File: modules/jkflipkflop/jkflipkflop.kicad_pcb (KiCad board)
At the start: 2 copper layers, 52.1 x 53.6 mm, 101 parts, among them J1 Conn_02x18_Counter_Clockwise, Q1 DMP3099L, Q10 2N7002, Q11 DMP3099L, Q12 DMP3099L, Q13 DMP3099L, Q14 2N7002, Q15 2N7002, Q16 2N7002, Q17 DMP3099L, Q18 DMP3099L, Q19 DMP3099L, Q2 2N7002, Q20 2N7002, Q21 2N7002, Q22 2N7002, Q23 DMP3099L, Q24 DMP3099L, Q25 DMP3099L, Q26 2N7002, Q27 2N7002, Q28 2N7002, Q29 DMP3099L, Q3 2N7002, Q30 DMP3099L, Q31 DMP3099L, Q32 2N7002, Q33 2N7002, Q34 2N7002, Q35 DMP3099L, Q36 DMP3099L, Q37 DMP3099L, Q38 2N7002, Q39 2N7002, Q4 2N7002, Q40 2N7002, Q41 DMP3099L, Q42 DMP3099L, Q43 DMP3099L, Q44 2N7002, Q45 2N7002, Q46 2N7002, Q47 DMP3099L, Q48 DMP3099L, Q49 DMP3099L, Q5 DMP3099L, Q50 DMP3099L, Q51 2N7002, Q52 2N7002, Q53 2N7002, Q54 2N7002, Q55 2N7002, Q56 2N7002, Q57 DMP3099L, Q58 DMP3099L, Q59 DMP3099L, Q6 DMP3099L, Q60 DMP3099L, Q61 DMP3099L, Q62 DMP3099L, Q63 2N7002, Q64 2N7002, Q65 2N7002, Q66 2N7002, Q67 2N7002, Q68 2N7002, Q69 DMP3099L, Q7 DMP3099L, Q70 DMP3099L, Q71 DMP3099L, Q72 DMP3099L, Q73 DMP3099L, Q74 DMP3099L, Q75 2N7002, Q76 2N7002, Q77 2N7002, Q78 2N7002, Q79 2N7002, Q8 2N7002, Q80 2N7002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

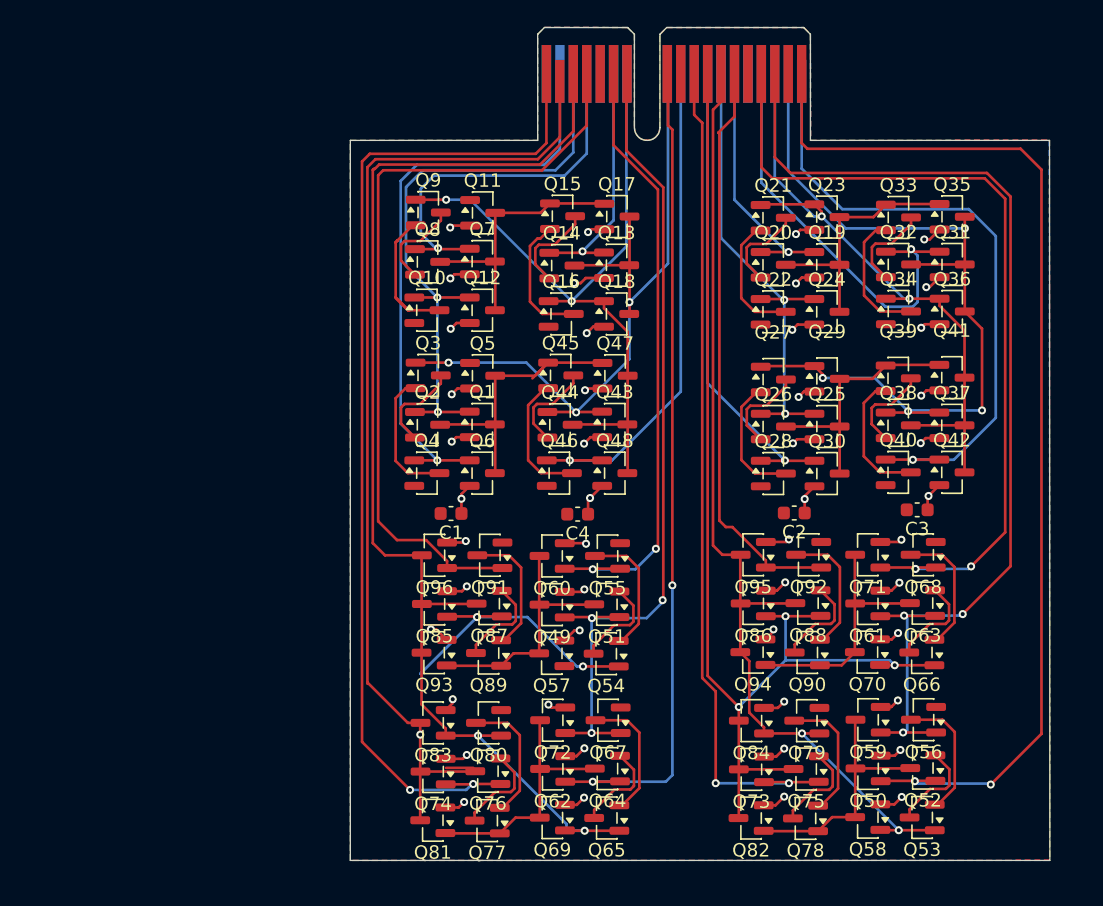
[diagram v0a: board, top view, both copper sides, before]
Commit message: changed from pcie x1 to mini pcie. added 2 flipflops
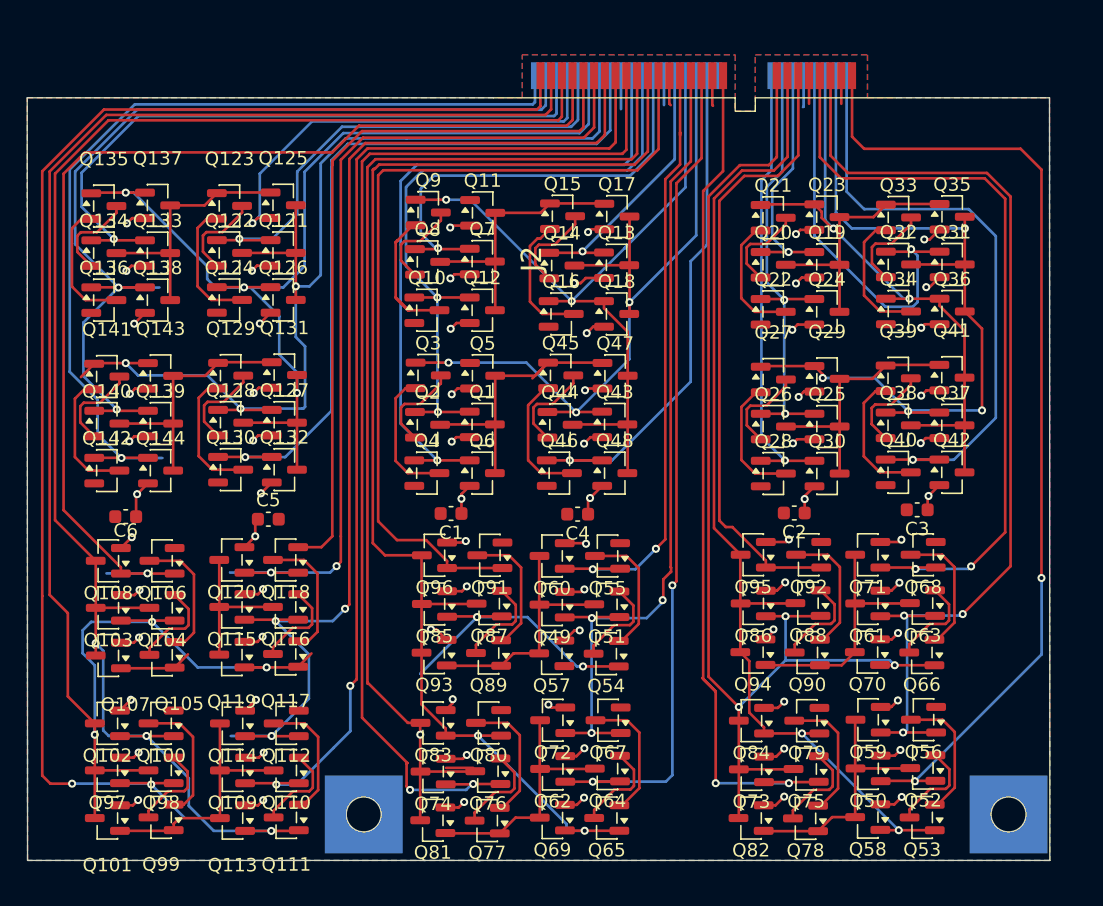
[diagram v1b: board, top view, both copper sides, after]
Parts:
- removed J1: Conn_02x18_Counter_Clockwise, Connector_PCBEdge:BUS_PCIexpress_x1
- added C5: 100n, Capacitor_SMD:C_0603_1608Metric, F.Cu at (68.9, 73.0)
- added C6: 100n, Capacitor_SMD:C_0603_1608Metric, F.Cu at (58.3, 72.8)
- added J2: Conn_02x26_Odd_Even, mpcie:mpcie-full-card, F.Cu at (100.7, 38.5)
- added Q100: 2N7002, Package_TO_SOT_SMD:SOT-23, F.Cu at (60.9, 88.2)
- added Q101: DMP3099L, Package_TO_SOT_SMD:SOT-23, F.Cu at (56.9, 95.3)
- added Q102: DMP3099L, Package_TO_SOT_SMD:SOT-23, F.Cu at (56.9, 88.2)
- added Q103: DMP3099L, Package_TO_SOT_SMD:SOT-23, F.Cu at (57.0, 79.6)
- added Q104: 2N7002, Package_TO_SOT_SMD:SOT-23, F.Cu at (61.0, 79.6)
- added Q105: 2N7002, Package_TO_SOT_SMD:SOT-23, F.Cu at (61.0, 83.1)
- added Q106: 2N7002, Package_TO_SOT_SMD:SOT-23, F.Cu at (61.0, 76.1)
- added Q107: DMP3099L, Package_TO_SOT_SMD:SOT-23, F.Cu at (57.0, 83.2)
- added Q108: DMP3099L, Package_TO_SOT_SMD:SOT-23, F.Cu at (57.0, 76.1)
- added Q109: DMP3099L, Package_TO_SOT_SMD:SOT-23, F.Cu at (66.2, 91.7)
- added Q110: 2N7002, Package_TO_SOT_SMD:SOT-23, F.Cu at (70.2, 91.7)
- added Q111: 2N7002, Package_TO_SOT_SMD:SOT-23, F.Cu at (70.2, 95.2)
- added Q112: 2N7002, Package_TO_SOT_SMD:SOT-23, F.Cu at (70.2, 88.2)
- added Q113: DMP3099L, Package_TO_SOT_SMD:SOT-23, F.Cu at (66.2, 95.3)
- added Q114: DMP3099L, Package_TO_SOT_SMD:SOT-23, F.Cu at (66.2, 88.2)
- added Q115: DMP3099L, Package_TO_SOT_SMD:SOT-23, F.Cu at (66.2, 79.6)
- added Q116: 2N7002, Package_TO_SOT_SMD:SOT-23, F.Cu at (70.2, 79.6)
- added Q117: 2N7002, Package_TO_SOT_SMD:SOT-23, F.Cu at (70.2, 83.1)
- added Q118: 2N7002, Package_TO_SOT_SMD:SOT-23, F.Cu at (70.2, 76.1)
- added Q119: DMP3099L, Package_TO_SOT_SMD:SOT-23, F.Cu at (66.2, 83.1)
- added Q120: DMP3099L, Package_TO_SOT_SMD:SOT-23, F.Cu at (66.2, 76.1)
- added Q121: DMP3099L, Package_TO_SOT_SMD:SOT-23, F.Cu at (70.0, 53.2)
- added Q122: 2N7002, Package_TO_SOT_SMD:SOT-23, F.Cu at (66.0, 53.2)
- added Q123: 2N7002, Package_TO_SOT_SMD:SOT-23, F.Cu at (66.0, 49.7)
- added Q124: 2N7002, Package_TO_SOT_SMD:SOT-23, F.Cu at (66.0, 56.7)
- added Q125: DMP3099L, Package_TO_SOT_SMD:SOT-23, F.Cu at (70.0, 49.7)
- added Q126: DMP3099L, Package_TO_SOT_SMD:SOT-23, F.Cu at (70.0, 56.7)
- added Q127: DMP3099L, Package_TO_SOT_SMD:SOT-23, F.Cu at (70.1, 65.8)
- added Q128: 2N7002, Package_TO_SOT_SMD:SOT-23, F.Cu at (66.1, 65.8)
- added Q129: 2N7002, Package_TO_SOT_SMD:SOT-23, F.Cu at (66.1, 62.3)
- added Q130: 2N7002, Package_TO_SOT_SMD:SOT-23, F.Cu at (66.1, 69.3)
- added Q131: DMP3099L, Package_TO_SOT_SMD:SOT-23, F.Cu at (70.1, 62.3)
- added Q132: DMP3099L, Package_TO_SOT_SMD:SOT-23, F.Cu at (70.1, 69.3)
- added Q133: DMP3099L, Package_TO_SOT_SMD:SOT-23, F.Cu at (60.7, 53.2)
- added Q134: 2N7002, Package_TO_SOT_SMD:SOT-23, F.Cu at (56.7, 53.2)
- added Q135: 2N7002, Package_TO_SOT_SMD:SOT-23, F.Cu at (56.7, 49.7)
- added Q136: 2N7002, Package_TO_SOT_SMD:SOT-23, F.Cu at (56.7, 56.7)
- added Q137: DMP3099L, Package_TO_SOT_SMD:SOT-23, F.Cu at (60.7, 49.7)
- added Q138: DMP3099L, Package_TO_SOT_SMD:SOT-23, F.Cu at (60.7, 56.7)
- added Q139: DMP3099L, Package_TO_SOT_SMD:SOT-23, F.Cu at (60.9, 65.9)
- added Q140: 2N7002, Package_TO_SOT_SMD:SOT-23, F.Cu at (56.9, 65.9)
- added Q141: 2N7002, Package_TO_SOT_SMD:SOT-23, F.Cu at (56.9, 62.4)
- added Q142: 2N7002, Package_TO_SOT_SMD:SOT-23, F.Cu at (56.9, 69.4)
- added Q143: DMP3099L, Package_TO_SOT_SMD:SOT-23, F.Cu at (60.9, 62.4)
- added Q144: DMP3099L, Package_TO_SOT_SMD:SOT-23, F.Cu at (60.9, 69.4)
- added Q97: DMP3099L, Package_TO_SOT_SMD:SOT-23, F.Cu at (56.9, 91.7)
- added Q98: 2N7002, Package_TO_SOT_SMD:SOT-23, F.Cu at (60.9, 91.7)
- added Q99: 2N7002, Package_TO_SOT_SMD:SOT-23, F.Cu at (60.9, 95.2)
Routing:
- net /jk-flipflop4/Q: track 0.00 -> 128.0 mm, vias 0 -> 3
- net /jk-flipflop4/\Q: track 0.00 -> 114.9 mm, vias 0 -> 3
- net /jk-flipflop4/Preset: track 0.00 -> 102.0 mm, vias 0 -> 2
- net /jk-flipflop4/CLK: track 0.00 -> 84.9 mm, vias 0 -> 3
- net /jk-flipflop4/Clr: track 0.00 -> 81.1 mm, vias 0 -> 1
- net /jk-flipflop5/Q: track 0.00 -> 81.1 mm, vias 0 -> 3
- net /jk-flipflop5/\Q: track 0.00 -> 79.5 mm, vias 0 -> 3
- net /jk-flipflop4/J: track 0.00 -> 78.4 mm, vias 0 -> 2
- net +3V3: track 78.0 -> 154.0 mm, vias 48 -> 72
- net /jk-flipflop5/CLK: track 0.00 -> 71.2 mm, vias 0 -> 2
- net /jk-flipflop5/K: track 0.00 -> 68.5 mm, vias 0 -> 1
- net /jk-flipflop4/K: track 0.00 -> 65.9 mm, vias 0 -> 2
- net GND: track 0.00 -> 63.1 mm
- net /jk-flipflop5/Clr: track 0.00 -> 56.2 mm, vias 0 -> 1
- net /jk-flipflop5/J: track 0.00 -> 49.7 mm, vias 0 -> 1
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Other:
- board size 52.1 x 53.6 mm -> 76.1 x 56.8 mm

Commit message: flipflop fab output
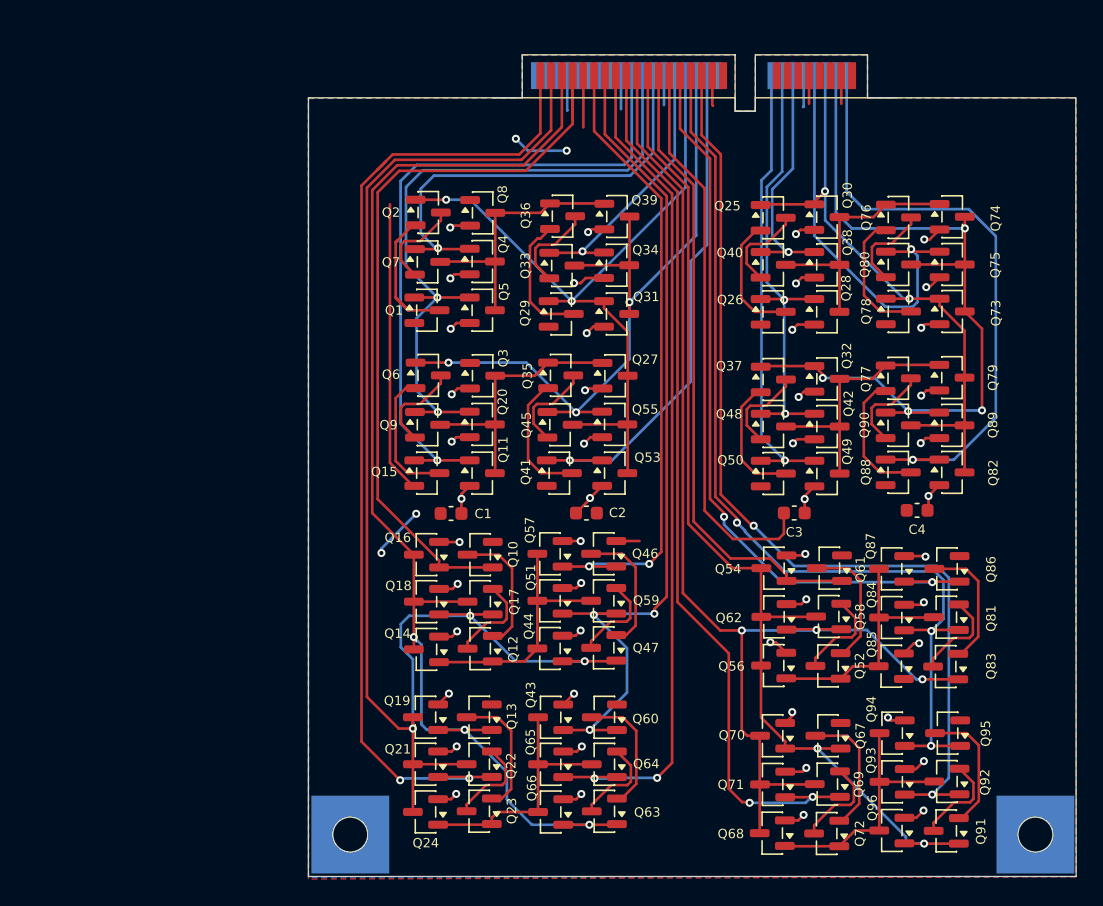
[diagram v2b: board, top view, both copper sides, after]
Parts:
- removed the C3 at (117.2, 72.3)
- removed C6: 100n, Capacitor_SMD:C_0603_1608Metric
- removed Q121, Q125, Q126, Q127, Q131, Q132, Q133, Q137, Q138, Q139, Q143, Q144: DMP3099L, Package_TO_SOT_SMD:SOT-23
- removed Q122, Q123, Q124, Q128, Q129, Q130, Q134, Q135, Q136, Q140, Q141, Q142: 2N7002, Package_TO_SOT_SMD:SOT-23
- removed the Q50 at (113.5, 91.6)
- removed the Q52 at (117.6, 91.5)
- removed the Q53 at (117.6, 95.2)
- removed the Q56 at (117.7, 88.0)
- removed the Q58 at (113.5, 95.2)
- removed the Q59 at (113.5, 88.0)
- removed the Q61 at (113.5, 79.3)
- removed the Q63 at (117.6, 79.3)
- removed the Q66 at (117.5, 82.9)
- removed the Q68 at (117.6, 75.7)
- removed the Q70 at (113.5, 82.9)
- removed the Q71 at (113.5, 75.7)
- removed the Q73 at (104.9, 91.6)
- removed the Q75 at (108.9, 91.6)
- removed the Q78 at (108.9, 95.3)
- removed the Q79 at (109.0, 88.0)
- removed the Q82 at (104.8, 95.3)
- removed the Q84 at (104.9, 88.0)
- removed the Q86 at (105.0, 79.3)
- removed the Q88 at (109.1, 79.3)
- removed the Q90 at (109.0, 82.9)
- removed the Q92 at (109.1, 75.7)
- removed the Q94 at (105.0, 82.9)
- removed the Q95 at (105.0, 75.7)
- Q11: renamed from Q6; value DMP3099L -> AO3401A
- Q14: renamed from Q107; value DMP3099L -> AO3401A
- Q16: renamed from Q108; value DMP3099L -> AO3401A
- Q18: renamed from Q103; value DMP3099L -> AO3401A
- Q19: renamed from Q102; value DMP3099L -> AO3401A
- Q20: renamed from Q1; value DMP3099L -> AO3401A
- Q21: renamed from Q97; value DMP3099L -> AO3401A
- Q24: renamed from Q101; value DMP3099L -> AO3401A
- Q27: renamed from Q47; value DMP3099L -> AO3401A
- Q28: renamed from Q24; value DMP3099L -> AO3401A
- Q3: renamed from Q5; value DMP3099L -> AO3401A
- Q30: renamed from Q23; value DMP3099L -> AO3401A
- Q31: renamed from Q18; value DMP3099L -> AO3401A
- Q32: renamed from Q29; value DMP3099L -> AO3401A
- Q34: renamed from Q13; value DMP3099L -> AO3401A
- Q38: renamed from Q19; value DMP3099L -> AO3401A
- Q39: renamed from Q17; value DMP3099L -> AO3401A
- Q4: renamed from Q7; value DMP3099L -> AO3401A
- Q42: renamed from Q25; value DMP3099L -> AO3401A
- Q43: renamed from Q114; value DMP3099L -> AO3401A
- Q44: renamed from Q119; value DMP3099L -> AO3401A
- Q49: renamed from Q30; value DMP3099L -> AO3401A
- Q5: renamed from Q12; value DMP3099L -> AO3401A
- Q51: renamed from Q115; value DMP3099L -> AO3401A
- Q53: renamed from Q48; value DMP3099L -> AO3401A
- Q54: renamed from Q96; value DMP3099L -> AO3401A
- Q55: renamed from Q43; value DMP3099L -> AO3401A
- Q56: renamed from Q93; value DMP3099L -> AO3401A
- Q57: renamed from Q120; value DMP3099L -> AO3401A
- Q62: renamed from Q85; value DMP3099L -> AO3401A
- Q65: renamed from Q109; value DMP3099L -> AO3401A
- Q66: renamed from Q113; value DMP3099L -> AO3401A
- Q68: renamed from Q81; value DMP3099L -> AO3401A
- Q70: renamed from Q83; value DMP3099L -> AO3401A
- Q71: renamed from Q74; value DMP3099L -> AO3401A
- Q73: renamed from Q36; value DMP3099L -> AO3401A
- Q74: renamed from Q35; value DMP3099L -> AO3401A
- Q75: renamed from Q31; value DMP3099L -> AO3401A
- Q79: renamed from Q41; value DMP3099L -> AO3401A
- Q8: renamed from Q11; value DMP3099L -> AO3401A
- Q82: renamed from Q42; value DMP3099L -> AO3401A
- Q84: renamed from Q49; value DMP3099L -> AO3401A
- Q85: renamed from Q57; value DMP3099L -> AO3401A
- Q87: renamed from Q60; value DMP3099L -> AO3401A
- Q89: renamed from Q37; value DMP3099L -> AO3401A
- Q93: renamed from Q62; value DMP3099L -> AO3401A
- Q94: renamed from Q72; value DMP3099L -> AO3401A
- Q96: renamed from Q69; value DMP3099L -> AO3401A
- moved Q52 25.3 mm to (110.6, 83.9)
- moved Q54 25.3 mm to (106.5, 76.7)
- moved Q56 25.3 mm to (106.5, 83.9)
- moved Q58 25.3 mm to (110.6, 80.3)
- moved Q61 25.3 mm to (110.7, 76.7)
- moved Q62 25.3 mm to (106.5, 80.3)
- moved Q67 25.3 mm to (110.6, 89.1)
- moved Q68 25.3 mm to (106.4, 96.4)
- moved Q69 25.3 mm to (110.5, 92.7)
- moved Q70 25.3 mm to (106.4, 89.1)
- moved Q71 25.3 mm to (106.4, 92.8)
- moved Q72 25.3 mm to (110.5, 96.4)
- moved Q81 25.3 mm to (119.4, 80.3)
- moved Q83 25.3 mm to (119.3, 84.0)
- moved Q84 25.3 mm to (115.3, 80.3)
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- renumbered C5 to C2, C2 to C3, J2 to J1, Q10 to Q1, Q106 to Q10, Q105 to Q12, Q100 to Q13, Q4 to Q15, Q104 to Q17, Q9 to Q2, Q98 to Q22, Q99 to Q23, Q21 to Q25, Q22 to Q26, Q16 to Q29, Q14 to Q33, Q45 to Q35, Q15 to Q36, Q27 to Q37, Q20 to Q40, Q46 to Q41, Q44 to Q45, Q118 to Q46, Q117 to Q47, Q26 to Q48, Q28 to Q50, Q89 to Q52, Q87 to Q58, Q116 to Q59, Q3 to Q6, Q112 to Q60, Q91 to Q61, Q111 to Q63, Q110 to Q64, Q80 to Q67, Q76 to Q69, Q8 to Q7, Q77 to Q72, Q33 to Q76, Q39 to Q77, Q34 to Q78, Q32 to Q80, Q51 to Q81, Q54 to Q83, Q55 to Q86, Q40 to Q88, Q2 to Q9, Q38 to Q90, Q65 to Q91, Q64 to Q92, Q67 to Q95
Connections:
- J1 pad 1: /jk-flipflop2/J -> unconnected-(J2-Pin_1-Pad1)
- J1 pad 11: /jk-flipflop2/Clr -> unconnected-(J2-Pin_11-Pad11)
- J1 pad 13: /jk-flipflop2/\Q -> unconnected-(J2-Pin_13-Pad13)
- J1 pad 15: /jk-flipflop2/Q -> unconnected-(J2-Pin_15-Pad15)
- J1 pad 17: /jk-flipflop2/Preset -> unconnected-(J2-Pin_17-Pad17)
- J1 pad 38: /jk-flipflop5/Clr -> unconnected-(J2-Pin_38-Pad38)
- J1 pad 40: /jk-flipflop5/Q -> unconnected-(J2-Pin_40-Pad40)
- J1 pad 42: /jk-flipflop5/\Q -> unconnected-(J2-Pin_42-Pad42)
- J1 pad 44: /jk-flipflop5/Preset -> unconnected-(J2-Pin_44-Pad44)
- J1 pad 48: /jk-flipflop5/J -> unconnected-(J2-Pin_48-Pad48)
- J1 pad 5: /jk-flipflop2/CLK -> unconnected-(J2-Pin_5-Pad5)
- J1 pad 50: /jk-flipflop5/CLK -> unconnected-(J2-Pin_50-Pad50)
- J1 pad 52: /jk-flipflop5/K -> unconnected-(J2-Pin_52-Pad52)
- J1 pad 7: /jk-flipflop2/K -> unconnected-(J2-Pin_7-Pad7)
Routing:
- net /jk-flipflop2/Q: track 88.2 -> 0.00 mm, vias 3 -> 0
- net /jk-flipflop5/Q: track 81.1 -> 0.00 mm, vias 3 -> 0
- net /jk-flipflop5/\Q: track 79.5 -> 0.00 mm, vias 3 -> 0
- net /jk-flipflop2/\Q: track 76.6 -> 0.00 mm, vias 2 -> 0
- net /jk-flipflop2/CLK: track 74.6 -> 0.00 mm, vias 3 -> 0
- net /jk-flipflop2/J: track 73.4 -> 0.00 mm, vias 2 -> 0
- net /jk-flipflop5/CLK: track 71.2 -> 0.00 mm, vias 2 -> 0
- net /jk-flipflop5/K: track 68.5 -> 0.00 mm, vias 1 -> 0
- net +3V3: track 154.0 -> 86.0 mm, vias 72 -> 48
- net /jk-flipflop2/Preset: track 64.6 -> 0.00 mm, vias 2 -> 0
- net /jk-flipflop2/K: track 57.9 -> 0.00 mm, vias 2 -> 0
- net /jk-flipflop5/Clr: track 56.2 -> 0.00 mm, vias 1 -> 0
- net /jk-flipflop5/J: track 49.7 -> 0.00 mm, vias 1 -> 0
- net /jk-flipflop2/Clr: track 46.4 -> 0.00 mm
- net /jk-flipflop5/Preset: track 38.1 -> 0.00 mm, vias 1 -> 0
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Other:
- board size 76.1 x 56.8 mm -> 57.2 x 61.2 mm
